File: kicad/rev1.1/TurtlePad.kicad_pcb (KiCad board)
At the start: 2 copper layers, 111.1 x 41.3 mm, 15 parts, among them SW1 SW_Push, U1 ProMicro

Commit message: Added designer silkscreen
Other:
- board text added: "TurtlePad rev1.1 Designed by ItsFiremanSam"
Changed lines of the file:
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@@
     )
     (pad_to_mask_clearance 0)
+    (grid_origin 175.41875 116.763439)
     (pcbplotparams
       (layerselection 0x00010fc_ffffffff)
@@
   (gr_line (start 100.421561 79.600939) (end 206.784061 79.600939) (layer "Edge.Cuts") (width 0.05))
   (gr_arc (start 206.784061 79.600939) (mid 208.467859 80.298391) (end 209.165311 81.982189) (layer "Edge.Cuts") (width 0.05))
+  (gr_text "TurtlePad rev1.1\nDesigned by ItsFiremanSam" (at 174.625 115.969689) (layer "B.SilkS")
+    (effects (font (size 1 1) (thickness 0.2)) (justify mirror))
+  )
   (segment (start 151.077811 116.400939) (end 150.934061 116.400939) (width 0.254) (layer "F.Cu") (net 2))
   (segment (start 121.117811 107.223439) (end 120.106561 106.212189) (width 0.254) (layer "B.Cu") (net 2))

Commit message: rev1.1 again
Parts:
- added G***: LOGO, LOGO, B.Cu at (120.7, 110.4)
- MX1, MX2, MX3, MX4, MX5, MX6, MX7, MX8: footprint MX_Only:MXOnly-1U-Hotswap -> 0xcb:SW_Cherry_MX_PCB_1.00u
- renumbered RGB4 to RGBe
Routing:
- net MX6: track 15.8 -> 18.8 mm
- net MX3: track 26.9 -> 29.2 mm
- net MX4: track 46.6 -> 48.9 mm
- net MX7: track 14.8 -> 16.5 mm
- net MX2: track 30.0 -> 31.4 mm
- net (no net): track 0.00 -> 0.85 mm
- net MX1: track 50.6 -> 51.2 mm

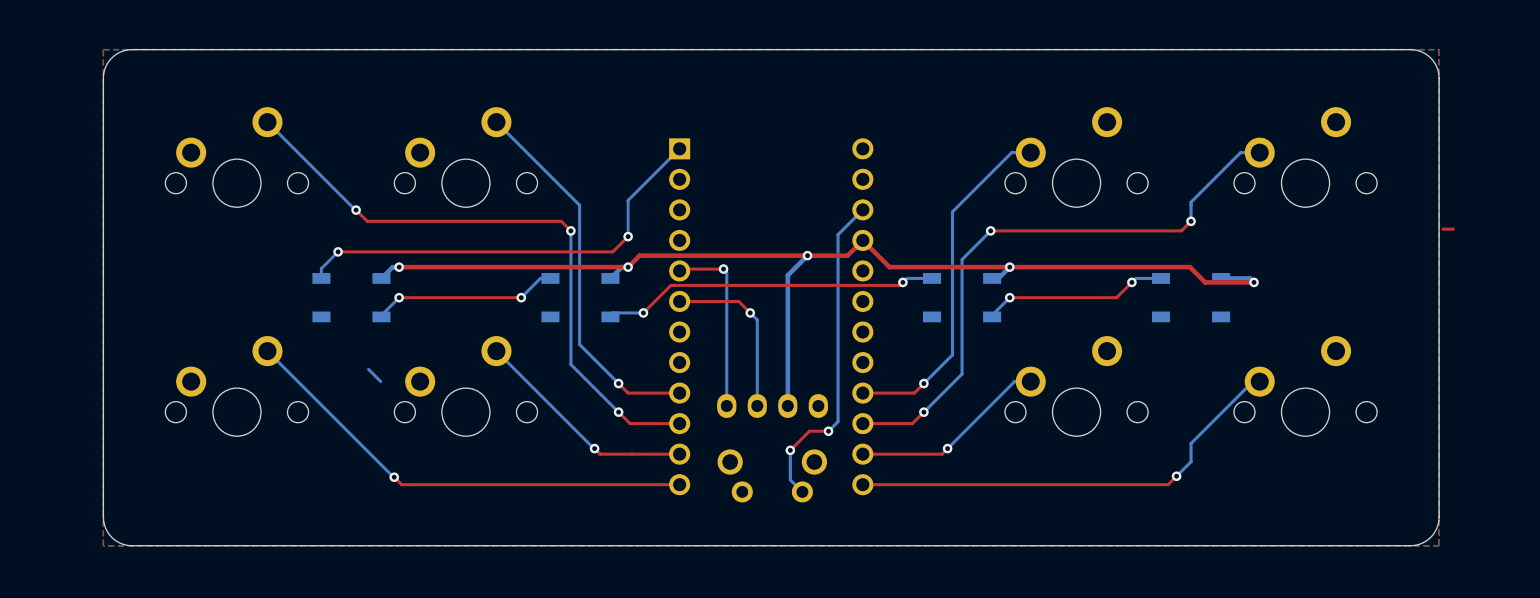
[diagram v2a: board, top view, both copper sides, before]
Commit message: cleaned up, rounded traces added teardrops
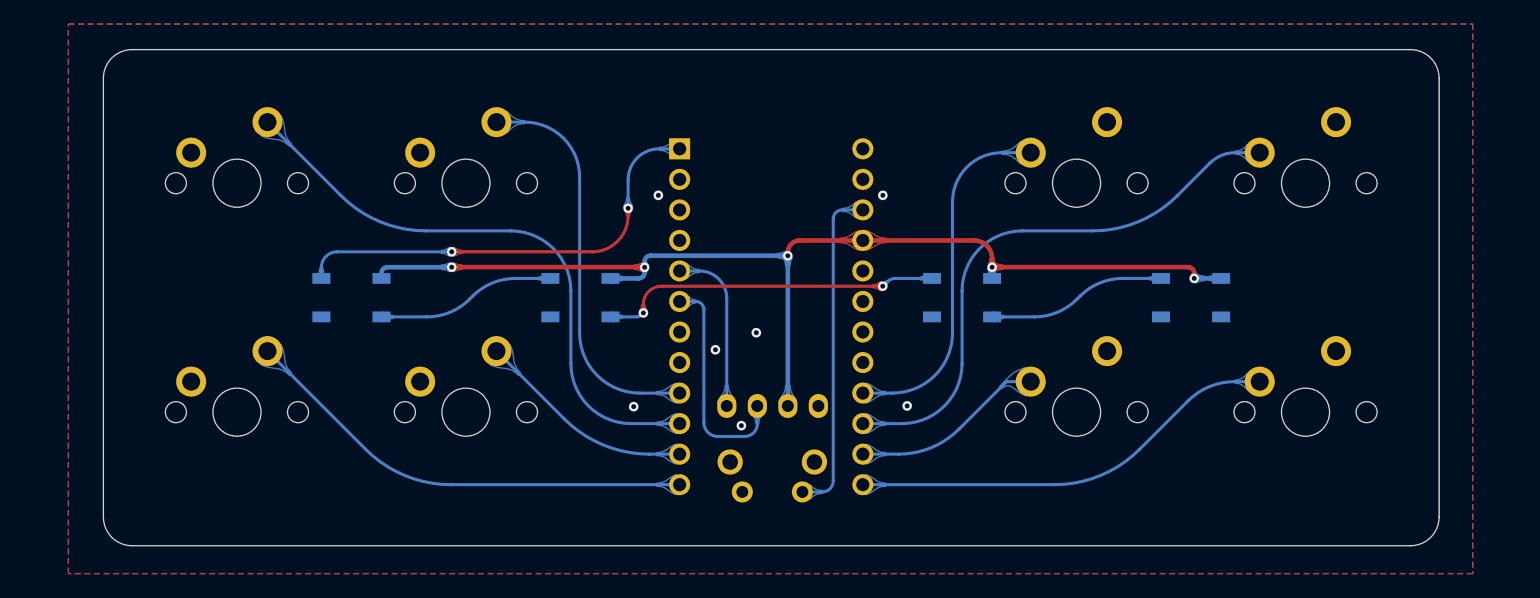
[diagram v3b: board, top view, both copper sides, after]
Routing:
- net SCL: track 14.3 -> 18.9 mm, vias 1 -> 0
- net VCC: track 95.1 -> 91.3 mm
- net MX4: track 48.9 -> 46.4 mm, vias 3 -> 0
- net MX1: track 51.2 -> 48.9 mm, vias 3 -> 0
- net MX2: track 31.4 -> 33.3 mm, vias 1 -> 0
- net MX8: track 37.5 -> 35.8 mm, vias 1 -> 0
- net GND: track 1.57 -> 0.14 mm, vias 0 -> 7
- net SDA: track 15.2 -> 14.1 mm, vias 1 -> 0
- net (no net): track 0.85 -> 0.00 mm
- net LED: track 36.5 -> 37.4 mm
- net Net-(RGB3-Pad2): track 15.5 -> 14.9 mm, vias 2 -> 0
- net Net-(RGB1-Pad2): track 15.5 -> 14.9 mm, vias 2 -> 0
- net MX5: track 38.9 -> 38.4 mm, vias 1 -> 0
- net MX6: track 18.8 -> 18.3 mm, vias 1 -> 0
- net MX3: track 29.2 -> 29.7 mm, vias 1 -> 0
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
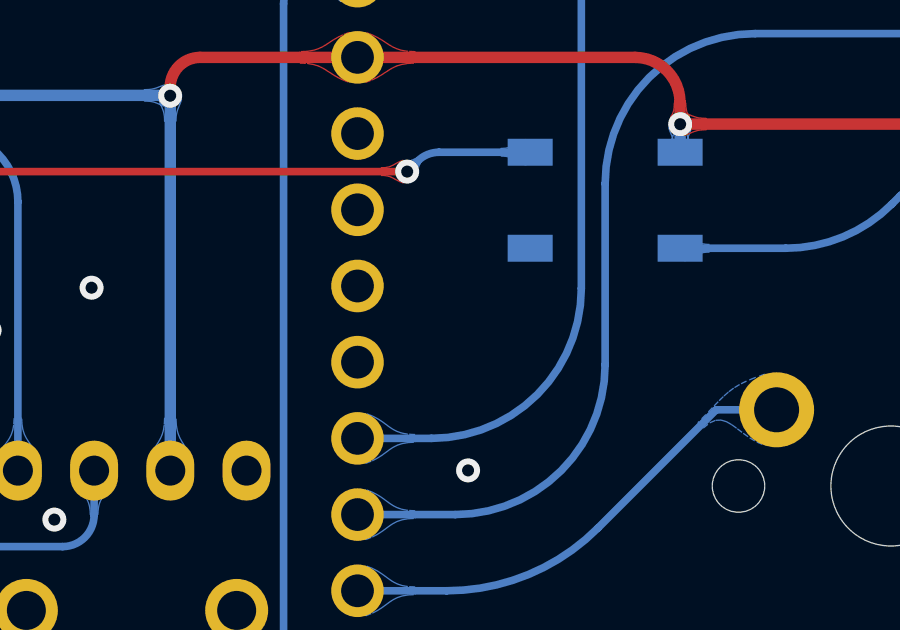
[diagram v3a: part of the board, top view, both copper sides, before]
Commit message: Fix LED without GND
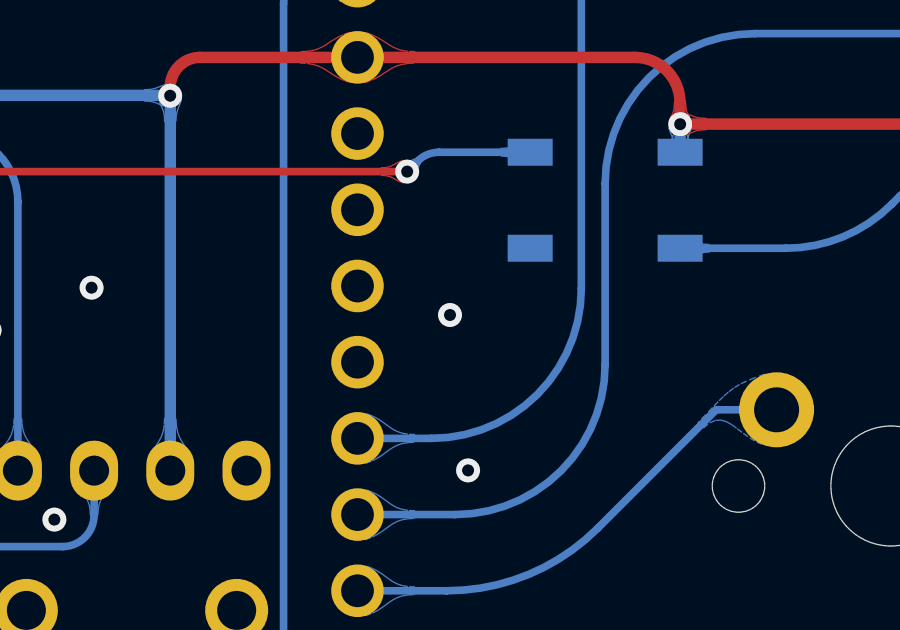
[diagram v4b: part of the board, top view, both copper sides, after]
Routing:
- net GND: vias 7 -> 8
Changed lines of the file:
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@@
   (via (at 164.90875 109.243439) (size 0.8) (drill 0.4) (layers "F.Cu" "B.Cu") (free) (net 2))
   (via (at 148.95875 104.573439) (size 0.8) (drill 0.4) (layers "F.Cu" "B.Cu") (free) (net 2))
+  (via (at 164.30625 104.063439) (size 0.8) (drill 0.4) (layers "F.Cu" "B.Cu") (free) (net 2))
   (via (at 162.88875 91.723439) (size 0.8) (drill 0.4) (layers "F.Cu" "B.Cu") (free) (net 2))
   (via (at 151.11875 110.883439) (size 0.8) (drill 0.4) (layers "F.Cu" "B.Cu") (free) (net 2))

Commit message: plates
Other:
- board size 111.1 x 41.3 mm -> 120 x 42 mm
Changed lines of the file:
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@@
     (grid_origin 175.41875 116.763439)
     (pcbplotparams
-      (layerselection 0x00010fc_ffffffff)
+      (layerselection 0x00010c0_7ffffffe)
       (disableapertmacros false)
       (usegerberextensions false)
@@
       (svguseinch false)
       (svgprecision 6)
-      (excludeedgelayer true)
+      (excludeedgelayer false)
       (plotframeref false)
       (viasonmask false)
@@
       (hpglpenspeed 20)
       (hpglpendiameter 15.000000)
-      (dxfpolygonmode true)
-      (dxfimperialunits true)
+      (dxfpolygonmode false)
+      (dxfimperialunits false)
       (dxfusepcbnewfont true)
       (psnegative false)
@@
       (sketchpadsonfab false)
       (subtractmaskfromsilk true)
-      (outputformat 1)
+      (outputformat 3)
       (mirror false)
-      (drillshape 0)
+      (drillshape 2)
       (scaleselection 1)
       (outputdirectory "./gerbers")
@@
     )
   )
-  (gr_arc (start 209.165311 118.494689) (mid 208.467859 120.178487) (end 206.784061 120.875939) (layer "Edge.Cuts") (width 0.05))
-  (gr_arc (start 100.421561 120.875939) (mid 98.737763 120.178487) (end 98.040311 118.494689) (layer "Edge.Cuts") (width 0.05))
-  (gr_line (start 98.040311 118.494689) (end 98.040311 81.982189) (layer "Edge.Cuts") (width 0.05))
-  (gr_arc (start 98.040311 81.982189) (mid 98.737763 80.298391) (end 100.421561 79.600939) (layer "Edge.Cuts") (width 0.05))
-  (gr_line (start 209.165311 81.982189) (end 209.165311 118.494689) (layer "Edge.Cuts") (width 0.05))
-  (gr_line (start 206.784061 120.875939) (end 100.421561 120.875939) (layer "Edge.Cuts") (width 0.05))
-  (gr_line (start 100.421561 79.600939) (end 206.784061 79.600939) (layer "Edge.Cuts") (width 0.05))
-  (gr_arc (start 206.784061 79.600939) (mid 208.467859 80.298391) (end 209.165311 81.982189) (layer "Edge.Cuts") (width 0.05))
-  (gr_text "TurtlePad rev1.1\nDesigned by ItsFiremanSam" (at 196.05625 116.763439) (layer "B.SilkS")
+  (gr_arc (start 93.59875 84.243439) (mid 95.063216 80.707905) (end 98.59875 79.243439) (layer "Edge.Cuts") (width 0.25))
+  (gr_line (start 208.59875 79.243439) (end 98.59875 79.243439) (layer "Edge.Cuts") (width 0.25))
+  (gr_line (start 98.59875 121.243439) (end 208.59875 121.243439) (layer "Edge.Cuts") (width 0.25))
+  (gr_arc (start 213.59875 116.243439) (mid 212.134284 119.778973) (end 208.59875 121.243439) (layer "Edge.Cuts") (width 0.25))
+  (gr_arc (start 208.59875 79.243439) (mid 212.134284 80.707905) (end 213.59875 84.243439) (layer "Edge.Cuts") (width 0.25))
+  (gr_circle (center 98.09875 116.743439) (end 100.84875 116.743439) (layer "Edge.Cuts") (width 0.25) (fill none))
+  (gr_circle (center 209.09875 83.743439) (end 211.84875 83.743439) (layer "Edge.Cuts") (width 0.25) (fill none))
+  (gr_circle (center 209.09875 116.743439) (end 211.84875 116.743439) (layer "Edge.Cuts") (width 0.25) (fill none))
+  (gr_arc (start 98.59875 121.243439) (mid 95.063216 119.778973) (end 93.59875 116.243439) (layer "Edge.Cuts") (width 0.25))
+  (gr_line (start 93.59875 84.243439) (end 93.59875 116.243439) (layer "Edge.Cuts") (width 0.25))
+  (gr_circle (center 98.09875 83.743439) (end 100.84875 83.743439) (layer "Edge.Cuts") (width 0.25) (fill none))
+  (gr_line (start 213.59875 116.243439) (end 213.59875 84.243439) (layer "Edge.Cuts") (width 0.25))
+  (gr_text "TurtlePad rev1.1\nDesigned by ItsFiremanSam" (at 195.01875 116.773439) (layer "B.SilkS")
     (effects (font (size 1 1) (thickness 0.2)) (justify mirror))
   )
-  (segment (start 151.077811 116.400939) (end 150.934061 116.400939) (width 0.254) (layer "F.Cu") (net 2))
+  (gr_text "" (at 93.59875 122.263005) (layer "Edge.Cuts")
+    (effects (font (size 4.83362 3.04518) (thickness 0.604202)) (justify left top))
+  )
   (via (at 142.15875 109.303439) (size 0.8) (drill 0.4) (layers "F.Cu" "B.Cu") (free) (net 2))
   (via (at 152.35875 103.153439) (size 0.8) (drill 0.4) (layers "F.Cu" "B.Cu") (free) (net 2))
@@
   (arc (start 121.677171 97.703439) (mid 121.323618 97.849886) (end 121.177171 98.203439) (width 0.381) (layer "B.Cu") (net 3))
   (arc (start 143.06875 97.24225) (mid 143.215197 96.888697) (end 143.56875 96.74225) (width 0.381) (layer "B.Cu") (net 3))
-  (segment (start 161.222811 92.935939) (end 161.381561 92.935939) (width 0.254) (layer "F.Cu") (net 4))
   (segment locked (start 161.222811 92.935939) (end 159.514057 92.935939) (width 0.254) (layer "B.Cu") (net 4))
   (segment locked (start 157.840853 116.400939) (end 156.195 116.400939) (width 0.254) (layer "B.Cu") (net 4))
@@
   )
   (zone (net 2) (net_name "GND") (layers F&B.Cu) (hatch edge 0.508)
-    (connect_pads (clearance 0.508))
+    (connect_pads (clearance 0.35))
     (min_thickness 0.254) (filled_areas_thickness no)
-    (fill yes (thermal_gap 0.508) (thermal_bridge_width 0.508))
+    (fill yes (thermal_gap 0.35) (thermal_bridge_width 0.508))
     (polygon
       (pts
-        (xy 211.96875 123.193439)
-        (xy 95.12875 123.193439)
-        (xy 95.12875 77.473439)
-        (xy 211.96875 77.473439)
+        (xy 215.55875 123.193439)
+        (xy 91.43875 123.193439)
+        (xy 91.43875 77.473439)
+        (xy 215.55875 77.473439)
       )
     )
@@
     )
   )
+  (group "" (id 318871d7-fe55-4df2-b694-d22cc0c18ca2)
+    (members
+      1a4f133f-315b-407c-940b-018e4c3d2ab9
+      1ace53cb-b509-4366-b810-5f36bc4e8e2b
+      2bd71168-35fc-4719-825e-35c3ce08c848
+      33708f9d-5487-4311-bb50-5e6f39217080
+      3bc740ca-4b97-40bc-83e2-cb17c84d95f9
+      43de090f-4a74-4114-bf8b-0bcbe028afdd
+      48a2a59d-ad41-4441-b82e-4774fa3e8a69
+      4e33f3ad-b8a4-449d-b7c6-9094913fd872
+      86894629-da21-44f0-bfa8-d2d2666ab27e
+      8a759216-11c0-4eb1-9141-6080b7aaecfd
+      8de980a7-476b-482d-bb78-7e8e8527e0e2
+      c465beb6-9a07-43ad-95ac-3d7f2a3a626f
+      d0050567-81fc-4abd-8d92-ffb918472437
+    )
+  )

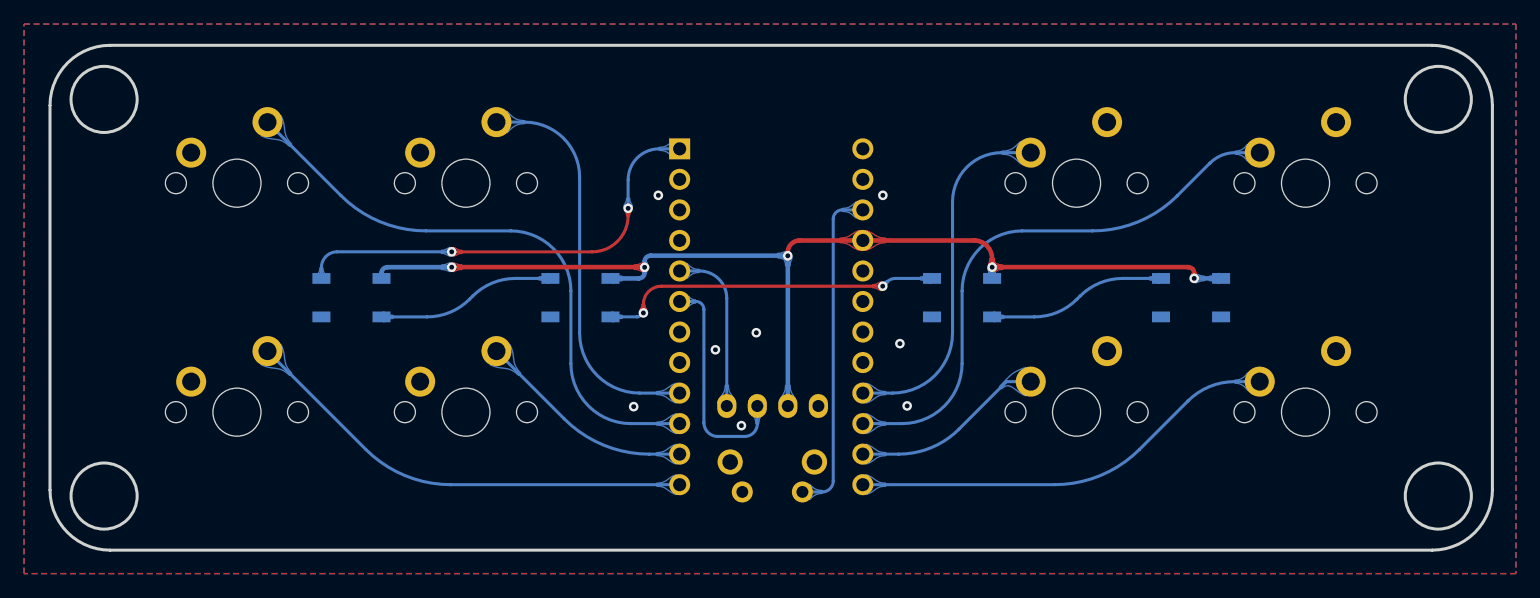
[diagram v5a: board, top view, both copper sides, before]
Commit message: changed PCB, added switch and bottom plate, added gerbers
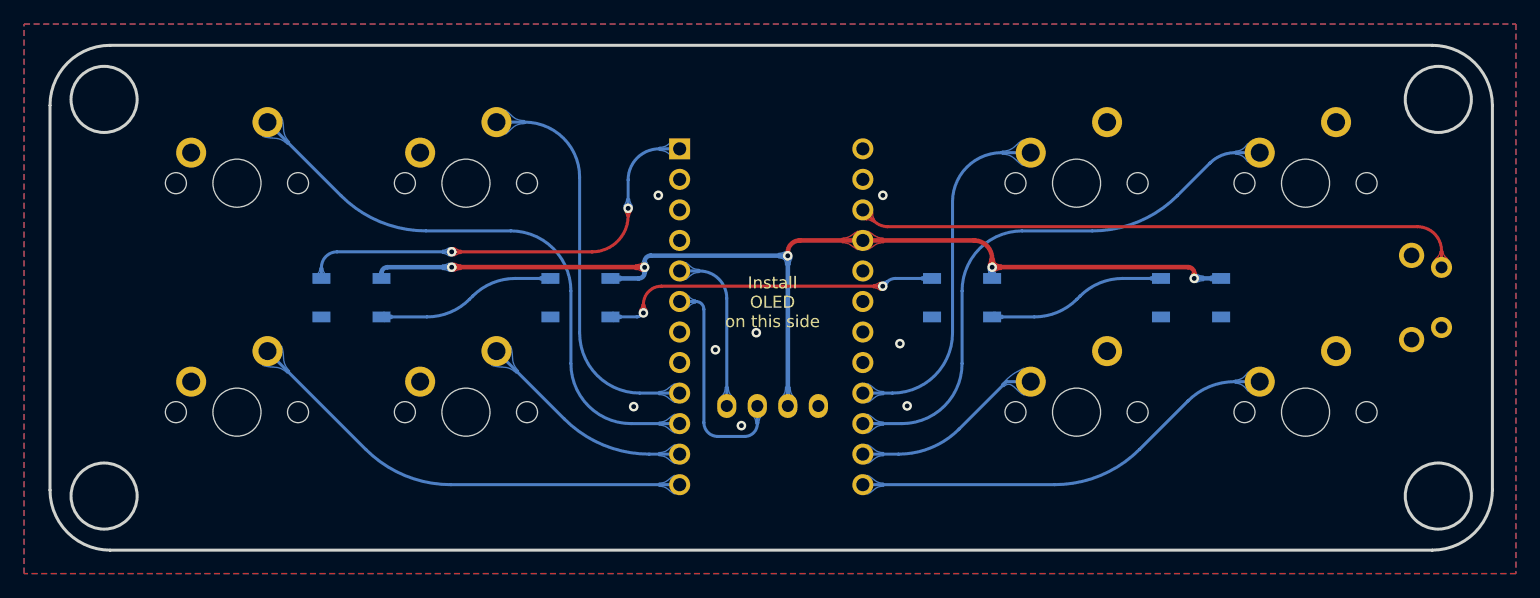
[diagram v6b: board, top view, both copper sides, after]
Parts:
- moved SW1 56.4 mm to (209.4, 97.7), turned to -90 degrees
- renumbered RGBe to RGB4
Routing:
- net reset: track 27.7 -> 51.1 mm
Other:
- board text added: "Install OLED on this side"
- board text added: "Install controller and reset button on this side"
